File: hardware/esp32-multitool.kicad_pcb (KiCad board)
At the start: 4 copper layers, 89 x 58 mm, 39 parts, among them J601 Conn_01x04, U1 XL1509-3.3, U2 XL1509-3.3, U202 XL1509-5, U3 RCLAMP0524P-N, U501 SN65HVD230DR, U502 ADuM1201AR

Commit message: block refactoring
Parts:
- removed C201: 180uF, Capacitor_SMD:C_0402_1005Metric
- removed C302: 10nF/50V, Capacitor_SMD:C_0402_1005Metric
- removed C306: 470uF/50V, Capacitor_SMD:C_0805_2012Metric
- removed C308: 4.7uF/50V, Capacitor_SMD:C_1206_3216Metric
- removed C504, C602, C604: 100nF, Capacitor_SMD:C_0402_1005Metric
- removed D201, D4, D6: B5819W, Diode_SMD:D_SOD-123
- removed D3: SMBJ6.0CA, Diode_SMD:D_SMB
- removed D302, D5: SS24FL, Diode_SMD:D_SOD-123F
- removed F2, F3, F4: ASMD1206-050, Fuse:Fuse_1206_3216Metric
- removed F301: mSMD050-60V, Fuse:Fuse_1812_4532Metric
- removed FB301: GZ2012D601TF, Inductor_SMD:L_0805_2012Metric
- removed J601: Conn_01x04, Connector_Phoenix_MC:PhoenixContact_MCV_1,5_4-G-3.81_1x04_P3.81mm_Vertical
- removed R213, R503: 10k, Resistor_SMD:R_0402_1005Metric
- removed R601, R602: 240R, Resistor_SMD:R_0805_2012Metric
- removed U1: XL1509-3.3, Package_SO:SOP-8_3.9x4.9mm_P1.27mm
- removed U202: XL1509-5, Package_SO:SOP-8_3.9x4.9mm_P1.27mm
- removed U501: SN65HVD230DR, Package_SO:SOIC-8_3.9x4.9mm_P1.27mm
- removed U502: ADuM1201AR, Package_SO:SOIC-8_3.9x4.9mm_P1.27mm
- added C10: 1nF, Capacitor_SMD:C_0603_1608Metric, F.Cu at (116.5, 66.4)
- added C11: 10nF, Capacitor_SMD:C_0603_1608Metric, F.Cu at (94.8, 95.3)
- added C14: 1uF, Capacitor_SMD:C_0603_1608Metric, F.Cu at (169.0, 93.1)
- added C15: 1uF, Capacitor_SMD:C_0603_1608Metric, F.Cu at (172.6, 93.1)
- added C7: 1uF, Capacitor_SMD:C_0603_1608Metric, F.Cu at (116.9, 81.9)
- added C8: 1uF, Capacitor_SMD:C_0603_1608Metric, F.Cu at (106.7, 81.9)
- added C9: 1uF, Capacitor_SMD:C_0603_1608Metric, F.Cu at (119.9, 84.2)
- added D10: D_SCHOTTKY_30V, Diode_SMD:D_SOD-123, F.Cu at (124.4, 103.3)
- added D12: D_TVS_30V, Diode_SMD:D_SMB, F.Cu at (121.2, 91.6)
- added D16: RCLAMP0502B, Package_TO_SOT_SMD:SOT-416, F.Cu at (166.8, 78.2)
- added D17: D_TVS_3V3, Diode_SMD:D_SOD-123, F.Cu at (161.3, 78.2)
- added D19: RCLAMP0502B, Package_TO_SOT_SMD:SOT-416, F.Cu at (116.2, 70.2)
- added D20: D_SCHOTTKY_30V, Diode_SMD:D_SOD-123, F.Cu at (168.4, 99.4)
- added D21: D_SCHOTTKY_30V, Diode_SMD:D_SOD-123, F.Cu at (168.2, 96.9)
- added D22: D_SCHOTTKY_30V, Diode_SMD:D_SOD-123, F.Cu at (173.4, 99.4)
- added D23: D_SCHOTTKY_30V, Diode_SMD:D_SOD-123, F.Cu at (173.4, 96.9)
- added D8: D_TVS_30V, Diode_SMD:D_SMB, F.Cu at (107.0, 90.6)
- added J1: Conn_01x03/1Wire, Connector_PinHeader_1.00mm:PinHeader_1x03_P1.00mm_Vertical, F.Cu at (114.4, 74.9)
- added J2: Conn_01x04/QWiiC, Connector_JST:JST_PH_B4B-PH-K_1x04_P2.00mm_Vertical, F.Cu at (161.3, 67.5)
- added J3: Conn_01x04/QWiiC, Connector_JST:JST_PH_B4B-PH-K_1x04_P2.00mm_Vertical, F.Cu at (161.3, 73.5)
- added J4: Conn_01x02/VIN, TerminalBlock_TE-Connectivity:TerminalBlock_TE_282834-2_1x02_P2.54mm_Horizontal, F.Cu at (109.5, 111.2)
- added J5: Conn_01x04/VIN_PROTECTED, Connector_PinHeader_1.00mm:PinHeader_1x04_P1.00mm_Vertical, F.Cu at (101.3, 106.3)
- added J6: Conn_01x02/DIN, TerminalBlock_TE-Connectivity:TerminalBlock_TE_282834-2_1x02_P2.54mm_Horizontal, F.Cu at (140.9, 111.3)
- added J7: Conn_01x02/AIN, TerminalBlock_TE-Connectivity:TerminalBlock_TE_282834-2_1x02_P2.54mm_Horizontal, F.Cu at (159.6, 111.4)
- added J8: Conn_01x02/PWM, TerminalBlock_TE-Connectivity:TerminalBlock_TE_282834-2_1x02_P2.54mm_Horizontal, F.Cu at (119.5, 111.3)
- added JP1: SolderJumper_3_Bridged12, Jumper:SolderJumper-3_P1.3mm_Bridged12_Pad1.0x1.5mm_NumberLabels, F.Cu at (127.1, 104.9)
- added JP3: SolderJumper_3_Bridged12, Jumper:SolderJumper-3_P1.3mm_Bridged12_Pad1.0x1.5mm_NumberLabels, F.Cu at (112.3, 80.1)
- added JP5: SolderJumper_3_Bridged12, Jumper:SolderJumper-3_P1.3mm_Bridged12_Pad1.0x1.5mm_NumberLabels, F.Cu at (119.5, 68.1)
- added L1: 2.2uH, Inductor_SMD:L_1008_2520Metric, F.Cu at (98.3, 94.0)
- added Q2: AO3400A, Package_TO_SOT_SMD:SOT-23, F.Cu at (121.1, 102.2)
- added R1: 4.7k, Resistor_SMD:R_0603_1608Metric, F.Cu at (116.5, 68.1)
- added R10: 100k, Resistor_SMD:R_0603_1608Metric, F.Cu at (115.6, 89.3)
- added R11: 1M, Resistor_SMD:R_0603_1608Metric, F.Cu at (118.1, 87.5)
- added R12: 5.1K, Resistor_SMD:R_0603_1608Metric, F.Cu at (118.1, 84.2)
- added R14: 5.1K, Resistor_SMD:R_0603_1608Metric, F.Cu at (108.5, 81.9)
- added R15: 150, Resistor_SMD:R_0603_1608Metric, F.Cu at (121.7, 68.9)
- added R16: R10k, Resistor_SMD:R_0603_1608Metric, F.Cu at (97.3, 100.6)
- added R17: 49.9k, Resistor_SMD:R_0603_1608Metric, F.Cu at (94.0, 100.6)
- added R18: 9.53k, Resistor_SMD:R_0603_1608Metric, F.Cu at (91.5, 99.9)
- added R19: 1M, Resistor_SMD:R_0603_1608Metric, F.Cu at (108.5, 85.2)
- added R2: 2.7k, Resistor_SMD:R_0603_1608Metric, F.Cu at (169.1, 78.5)
- added R25: 100k, Resistor_SMD:R_0603_1608Metric, F.Cu at (169.8, 102.3)
- added R26: 1M, Resistor_SMD:R_0603_1608Metric, F.Cu at (169.0, 94.9)
- added R27: 100k, Resistor_SMD:R_0603_1608Metric, F.Cu at (171.3, 102.3)
- added R28: 1M, Resistor_SMD:R_0603_1608Metric, F.Cu at (172.6, 94.9)
- added R3: 2.7k, Resistor_SMD:R_0603_1608Metric, F.Cu at (164.8, 78.5)
- added R7: 10k, Resistor_SMD:R_0603_1608Metric, F.Cu at (119.1, 105.0)
- added R8: 100, Resistor_SMD:R_0603_1608Metric, F.Cu at (118.3, 102.5)
- added R9: 100k, Resistor_SMD:R_0603_1608Metric, F.Cu at (112.3, 89.3)
- added TP1: TestPoint, TestPoint:TestPoint_Pad_1.0x1.0mm, F.Cu at (121.9, 66.2)
- added U9: AOZ1280CI, Package_TO_SOT_SMD:SOT-23-6, F.Cu at (94.5, 97.9)
- C1, C4: value 470uF/50V -> 1uF; footprint Capacitor_SMD:C_0805_2012Metric -> Capacitor_SMD:C_0603_1608Metric
- C2: value 4.7uF/50V -> 4.7uF/30V; footprint Capacitor_SMD:C_1206_3216Metric -> Capacitor_SMD:C_0805_2012Metric
- C3: value 330uF -> 10uF; footprint Capacitor_SMD:C_0402_1005Metric -> Capacitor_SMD:C_0603_1608Metric
- C5: value 4.7uF/50V -> 1uF; footprint Capacitor_SMD:C_1206_3216Metric -> Capacitor_SMD:C_0603_1608Metric
- C6: value 330uF -> 1uF; footprint Capacitor_SMD:C_0402_1005Metric -> Capacitor_SMD:C_0603_1608Metric
- D1: value B5819W -> D_SCHOTTKY_30V
- D2: value SS24FL -> D_SMPS; footprint Diode_SMD:D_SOD-123F -> Diode_SMD:D_0805_2012Metric
- D301: value SMBJ33CA -> D_TVS_30V
- F1: value mSMD050-60V -> Fuse; footprint Fuse:Fuse_1812_4532Metric -> Fuse:Fuse_Bourns_MF-RG300
- U2: value XL1509-3.3 -> mini_esp32; footprint Package_SO:SOP-8_3.9x4.9mm_P1.27mm -> ESP32:ESP32_mini
- U3: value RCLAMP0524P-N -> LM393; footprint Package_DFN_QFN:Diodes_UDFN-10_1.0x2.5mm_P0.5mm -> Package_SO:SOP-8_3.9x4.9mm_P1.27mm
- moved C5 137.9 mm to (160.4, 80.4)
- moved U2 125.1 mm to (141.9, 76.7)
- moved C4 120.1 mm to (159.0, 74.8)
- moved D301 95.5 mm to (105.0, 111.2), turned to -90 degrees
- moved U3 90.3 mm to (113.4, 85.6)
- moved F1 89.0 mm to (112.2, 104.2), turned to 180 degrees
- moved C6 83.3 mm to (114.1, 70.0), turned to -90 degrees
- moved D1 83.0 mm to (104.0, 104.7), turned to -90 degrees
- moved C3 77.1 mm to (101.4, 95.5), turned to -90 degrees
- moved C1 76.5 mm to (141.7, 81.9), turned to 90 degrees
- moved C2 72.5 mm to (98.6, 98.6)
- moved D2 67.6 mm to (98.6, 96.5)
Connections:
- C1 pad 1: GND -> +5V
- C1 pad 2: /+5V -> GND
- C2 pad 1: /+5V -> /VIN_PROTECTED
- C3 pad 1: /+3.3V -> +5V
- C4 pad 1: GND -> +3.3V
- C4 pad 2: /canbus/CAN_VIN_PROTECTED -> GND
- C5 pad 1: /canbus/CAN_VIN_PROTECTED -> +3.3V
- C6 pad 1: /canbus/CAN_3V3 -> +3.3V
- D1 pad 1: Net-(D1-Pad1) -> /VIN_PROTECTED
- D1 pad 2: Net-(F301-Pad1) -> Net-(D1-A)
- D2 pad 1: Net-(U1-Pad2) -> /power/SMPS_LX
- D301 pad 1: Net-(F301-Pad1) -> Net-(D1-A)
- F1 pad 1: Net-(D3-Pad1) -> /power/VIN
- F1 pad 2: /+5V -> Net-(D1-A)
- U2 pad 1: /canbus/CAN_VIN_PROTECTED -> GND
- U2 pad 2: Net-(D5-Pad1) -> unconnected-(U2-RST-Pad2)
- U2 pad 3: /canbus/CAN_3V3 -> unconnected-(U2-NC-Pad3)
- U2 pad 4: GND -> unconnected-(U2-IO_36/SVP/A0-Pad4)
- U2 pad 5: GND -> unconnected-(U2-IO_39/SVN-Pad5)
- U2 pad 6: GND -> unconnected-(U2-IO_26/D0-Pad6)
- U2 pad 7: GND -> /AIN2
- U2 pad 8: GND -> unconnected-(U2-IO_18/D5-Pad8)
- U3 pad 1: Net-(F2-Pad1) -> /DIN1
- U3 pad 2: Net-(F3-Pad1) -> /digital_in/DIN_VREF
- U3 pad 3: GND -> Net-(D8-A1)
- U3 pad 4: Net-(F4-Pad1) -> GND
- U3 pad 5: unconnected-(U3-Pad5) -> Net-(D12-A1)
- U3 pad 6: unconnected-(U3-Pad6) -> /digital_in/DIN_VREF
- U3 pad 7: /canbus/CAN_L_PROTECTED -> /DIN2
- U3 pad 8: GND -> +3.3V
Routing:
- net +5V: track 0.00 -> 15.4 mm, vias 0 -> 2
- net /power/SMPS_LX: track 0.00 -> 8.77 mm
- net Net-(U9-FB): track 0.00 -> 4.53 mm
- net /VIN_PROTECTED: track 0.00 -> 4.50 mm
- net Net-(U9-EN): track 0.00 -> 2.12 mm
- net /power/SMPS_BST: track 0.00 -> 1.91 mm
- removed copper zone on B.Cu, net (none)
- removed copper zone on F.Cu, net (none)
- removed copper zone on In1.Cu, net (none)
- removed copper zone on In2.Cu, net (none)
- removed copper zone on In2.Cu, net /+3.3V
- removed copper zone on In2.Cu, net /canbus/CAN_3V3
- removed copper zone on F.Cu, net /power/SW
- removed copper zone on F.Cu, net /power/VIN_PROTECTED
- removed copper zone on B.Cu, net GND
- removed copper zone on F.Cu, net GND
- removed copper zone on In1.Cu, net GND
- removed copper zone on In2.Cu, net GND
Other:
- board size 89 x 58 mm -> 91 x 58 mm
- board text added: "- +"
- board text added: "5V"
- board text added: "Analog IN 0-24V"
- board text added: "Digital IN 0-24V: H=3.3V"
- board text added: "GND 3.3V SDA SCL"
- board text added: "I2C/QWiiC"
- board text added: "PWM"
- board text added: "SMPS 5V 1.2A"
- board text added: "Vin 6-24VDC"
- board text removed: "+"
- board text removed: "-"
- board text removed: "0"
- board text removed: "00 BOOT"
- board text removed: "01 TXD0"
- board text removed: "02 LED"
- board text removed: "03 RXD0"
- board text removed: "04 1-WIRE"
- board text removed: "1"
- board text removed: "12"
- board text removed: "12 TDI"
- board text removed: "12V"
- board text removed: "13"
- board text removed: "13 TCK"
- board text removed: "14"
- board text removed: "14 TMS"
- board text removed: "15"
- board text removed: "15 TDO"
- board text removed: "16"
- board text removed: "16 SDA"
- board text removed: "17"
- board text removed: "17 SCL"
- board text removed: "18"
- board text removed: "19"
- board text removed: "1Wire"
- board text removed: "2"
- board text removed: "21"
- board text removed: "22"
- board text removed: "23"
- board text removed: "25"
- board text removed: "26"
- board text removed: "27"
- board text removed: "3"
- board text removed: "3.3V"
- board text removed: "32"
- board text removed: "32 CAN_TX"
- board text removed: "33"
- board text removed: "33 OPTO_OUT"
- board text removed: "34"
- board text removed: "34 CAN_RX"
- board text removed: "35"
- board text removed: "35 OPTO_IN"
- board text removed: "3V3"
- board text removed: "4"
- board text removed: "5"
- board text removed: "6"
- board text removed: "7"
- board text removed: "8-32V"
- board text removed: "A"
- board text removed: "ANTENNA-KEEP OUT"
- board text removed: "B"
- board text removed: "BOOT"
- board text removed: "C"
- board text removed: "CAN 12V"
- board text removed: "CAN GND"
- board text removed: "CAN bus"
- board text removed: "CAN term"
- board text removed: "CANH"
- board text removed: "CANL"
- board text removed: "D"
- board text removed: "DQ"
- board text removed: "E"
- board text removed: "EN"
- board text removed: "F"
- board text removed: "G"
- board text removed: "GND"
- board text removed: "GND & 3.3V"
- board text removed: "GND Vext IN OUT"
- board text removed: "GPIO"
- board text removed: "GPIO FUNC"
- board text removed: "GPIO JTAG"
- board text removed: "GPIO headers"
- board text removed: "H"
- board text removed: "I"
- board text removed: "I/O"
- board text removed: "I2C"
- board text removed: "ISO_GND"
- board text removed: "ISO_IN"
- board text removed: "ISO_OUT"
- board text removed: "J"
- board text removed: "JLCJLCJLCJLC"
- board text removed: "K"
- board text removed: "L"
- board text removed: "M"
- board text removed: "N"
- board text removed: "NMEA 2000"
- board text removed: "O"
- board text removed: "Opto I/O"
- board text removed: "Opto- coupled GPIO"
- board text removed: "P"
- board text removed: "PWR"
- board text removed: "Panel tabs"
- board text removed: "Power"
- board text removed: "Q"
- board text removed: "Qwiic"
- board text removed: "R"
- board text removed: "RESET"
- board text removed: "Rev. 2.0.1"
- board text removed: "Revision 2.0.1"
- board text removed: "S"
- board text removed: "SCL"
- board text removed: "SDA"
- board text removed: "SH-ESP32"
- board text removed: "Sailor Hat with ESP32"
- board text removed: "T"
- board text removed: "USB"
- board text removed: "USB 5V"
- board text removed: "USB impedance controlled traces designed for the JLC7628 stackup"
- board text removed: "User I/O Header"
- board text removed: "VLink"
- board text removed: "VN"
- board text removed: "VP"
- board text removed: "V_ISO"
- board text removed: "Vin"
- board text removed: "Vin_Prot for Hat Daughter board"
- board text removed: "https://github.com/hatlabs/SH-ESP32-hardware/"

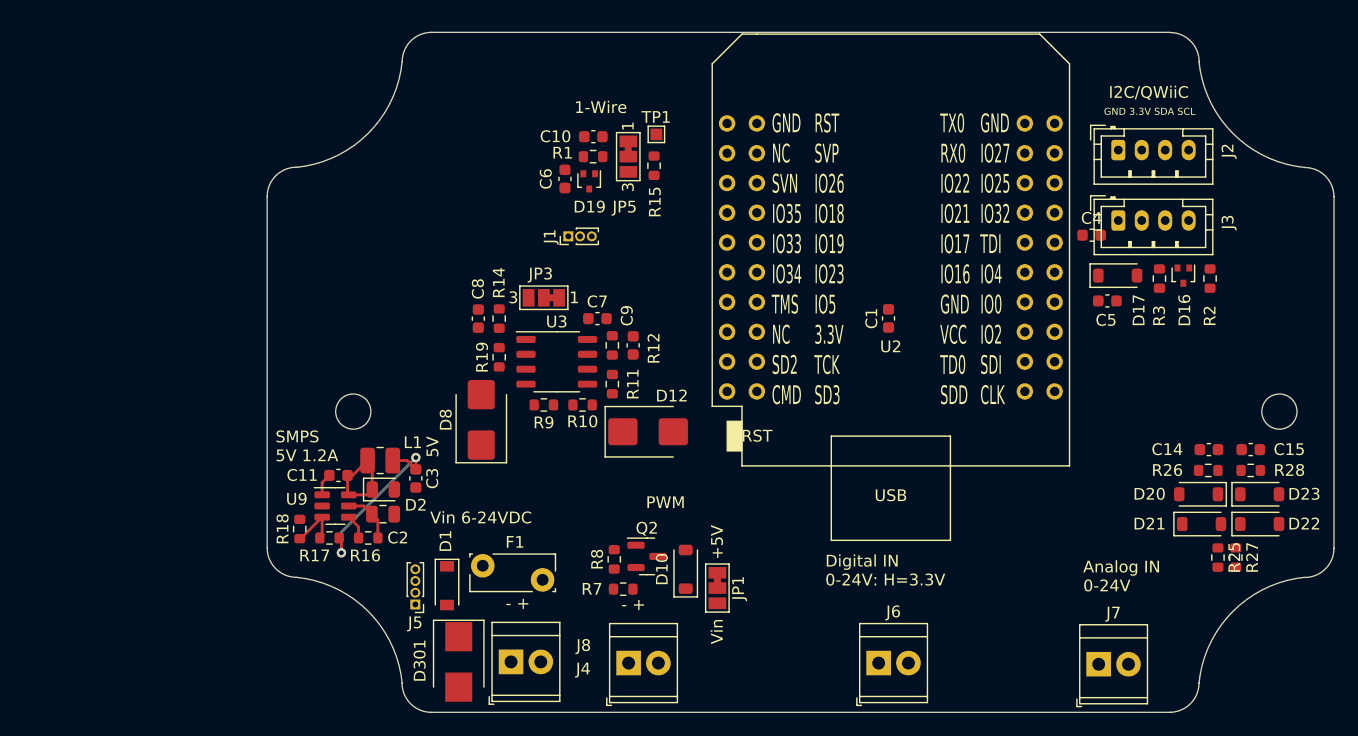
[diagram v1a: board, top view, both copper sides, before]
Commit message: moving subsheets to blocks
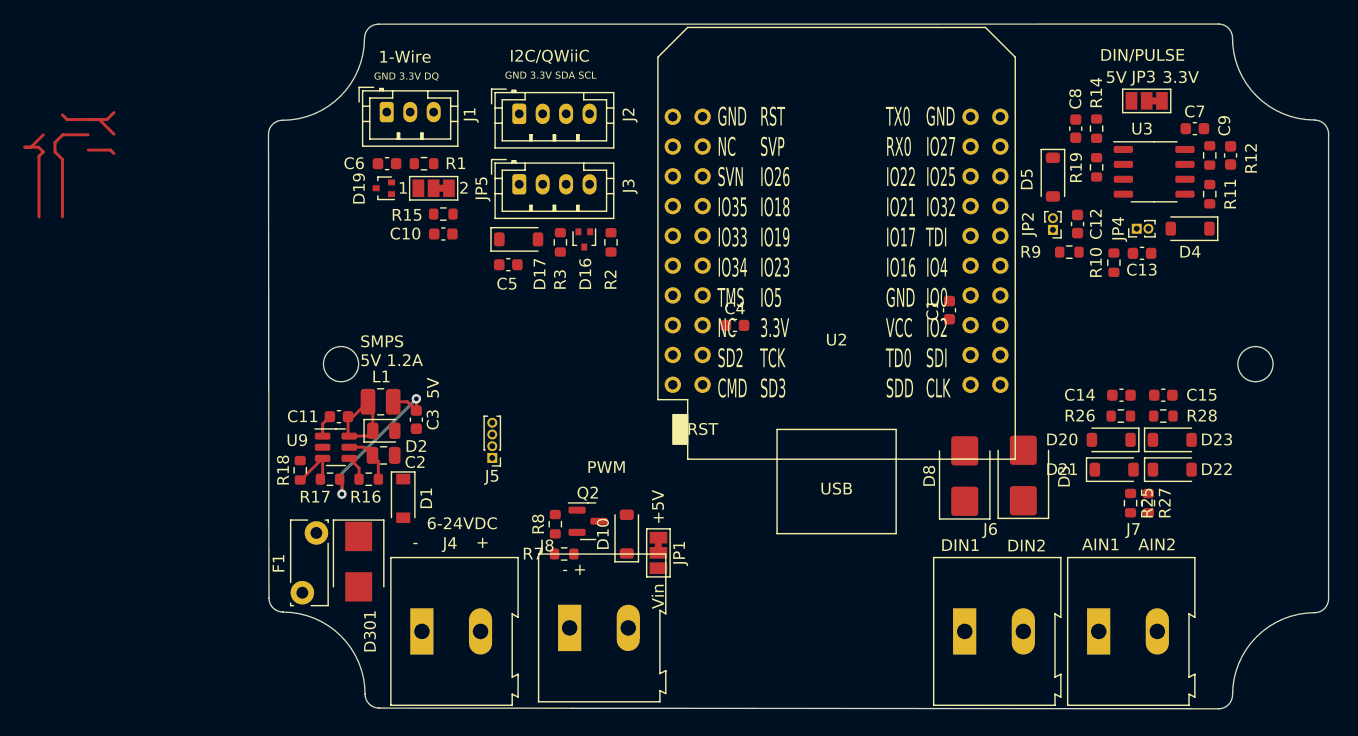
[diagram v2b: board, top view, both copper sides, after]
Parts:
- removed D12: D_TVS_30V, Diode_SMD:D_SMB
- removed TP1: TestPoint, TestPoint:TestPoint_Pad_1.0x1.0mm
- added C12: 22nF/30V, Capacitor_SMD:C_0603_1608Metric, F.Cu at (157.8, 73.8)
- added C13: 22nF/30V, Capacitor_SMD:C_0603_1608Metric, F.Cu at (163.3, 76.3)
- added D3: D_TVS_30V, Diode_SMD:D_SMB, F.Cu at (153.2, 95.3)
- added D4: D_SCHOTTKY_30V, Diode_SMD:D_SOD-123, F.Cu at (167.4, 74.2)
- added D5: D_SCHOTTKY_30V, Diode_SMD:D_SOD-123, F.Cu at (155.7, 69.8)
- added JP2: Jumper_2_Bridged, Connector_PinHeader_1.00mm:PinHeader_1x02_P1.00mm_Vertical, F.Cu at (155.7, 74.3)
- added JP4: Jumper_2_Bridged, Connector_PinHeader_1.00mm:PinHeader_1x02_P1.00mm_Vertical, F.Cu at (162.9, 74.2)
- J1: footprint Connector_PinHeader_1.00mm:PinHeader_1x03_P1.00mm_Vertical -> Connector_JST:JST_PH_B3B-PH-K_1x03_P2.00mm_Vertical
- J4, J6, J7, J8: footprint TerminalBlock_TE-Connectivity:TerminalBlock_TE_282834-2_1x02_P2.54mm_Horizontal -> TerminalBlock:TerminalBlock_Altech_AK300-2_P5.00mm
- moved JP3 54.1 mm to (163.7, 63.3)
- moved C7 53.5 mm to (167.8, 65.7)
- moved R14 53.5 mm to (159.4, 65.7)
- moved R19 53.5 mm to (159.4, 69.0)
- moved U3 53.5 mm to (164.4, 69.4)
- moved C8 53.5 mm to (157.7, 65.7)
- moved C9 53.5 mm to (170.9, 68.0)
- moved R11 53.5 mm to (169.1, 71.3)
- moved R12 53.5 mm to (169.1, 68.0)
- moved D16 51.2 mm to (115.7, 75.2)
- moved D17 51.2 mm to (110.2, 75.2)
- moved J2 51.2 mm to (110.2, 64.5)
- moved J3 51.2 mm to (110.2, 70.5)
- moved R2 51.2 mm to (118.0, 75.4)
- moved C5 51.2 mm to (109.3, 77.3)
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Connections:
- D8 pad 1: Net-(D8-A1) -> /digital_in/DIN_LINE1
- R10 pad 1: Net-(D12-A1) -> Net-(JP4-A)
- R11 pad 1: Net-(D12-A1) -> Net-(D4-K)
- R19 pad 1: Net-(D8-A1) -> Net-(D5-K)
- R9 pad 1: Net-(D8-A1) -> Net-(JP2-A)
- U3 pad 3: Net-(D8-A1) -> Net-(D5-K)
- U3 pad 5: Net-(D12-A1) -> Net-(D4-K)
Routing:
- net GND: track 0.00 -> 9.71 mm
- net +3.3V: track 0.00 -> 9.44 mm
- net /1WIRE_DQ: track 0.00 -> 7.53 mm
- net Net-(JP5-B): track 0.00 -> 2.32 mm
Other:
- board size 91 x 58 mm -> 90.4 x 58.4 mm
- board text added: "+"
- board text added: "-"
- board text added: "6-24VDC"
- board text added: "AIN1"
- board text added: "AIN2"
- board text added: "DIN/PULSE"
- board text added: "DIN1"
- board text added: "DIN2"
- board text added: "GND 3.3V DQ"
- board text removed: "Analog IN 0-24V"
- board text removed: "Digital IN 0-24V: H=3.3V"
- board text removed: "Vin 6-24VDC"
